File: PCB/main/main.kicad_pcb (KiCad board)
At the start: 2 copper layers, 100 x 100 mm, 46 parts, among them J1 Conn_01x33_Female, J2 Conn_01x33_Female, J3 Conn_01x33_Female, J4 Conn_01x33_Female, J5 USB_B_Micro, Q1 2N2222A, SW1 C13828, SW2 C13828, U1 TP4054, U2 MT3608L

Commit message: updated PCB & Assembly file
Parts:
- removed FTDI(UART)1: CH340C, CH340C:SOIC127P600X180-16N
- removed TSensor: LM75B, LM75BD:SOIC127P600X175-8N
- added FTDI1: CH340C, Package_SO:SOP-16_3.9x9.9mm_P1.27mm, F.Cu at (129.0, 78.8)
- added TempSensor1: LM75B, Package_SO:MSOP-8_3x3mm_P0.65mm, F.Cu at (133.5, 67.9)
- LDR1, LDR2, R1, R10, R11, R12, R13, R14, R15, R16, R17, R18, R19, R20, R5, R6, R7, R8, R9: footprint Resistor_SMD:R_0201_0603Metric -> Resistor_SMD:R_0603_1608Metric
- R2, R3, R4: value 100ohms -> 100; footprint Resistor_SMD:R_0201_0603Metric -> Resistor_SMD:R_0603_1608Metric
- moved J5 1.62 mm to (115.2, 92.7), turned to -90 degrees
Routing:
- net GND: track 83.8 -> 121.5 mm, vias 17 -> 18
- net +5V: track 0.00 -> 8.09 mm, vias 0 -> 2
- net /microcontroller_interfacing/USB Test Point: track 29.8 -> 23.0 mm, vias 0 -> 2
- net /PA8: track 135.9 -> 132.3 mm
- net USB D+: track 38.7 -> 35.1 mm
- net Net-(FTDI1-Pad13): track 67.5 -> 70.2 mm
- net /Power/Output: track 75.3 -> 77.8 mm
- net /PA9: track 50.4 -> 51.2 mm
- net /PA10: track 43.7 -> 44.5 mm
- net Net-(C4-Pad1): track 18.8 -> 19.6 mm
- net USB D-: track 34.6 -> 33.9 mm

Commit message: Updated PCB
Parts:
- LDR1, LDR2: footprint Resistor_SMD:R_0603_1608Metric -> Resistor_THT:R_Axial_DIN0204_L3.6mm_D1.6mm_P1.90mm_Vertical
- moved R19 4.74 mm to (129.5, 91.4)
- moved R14 2.89 mm to (149.9, 91.4)
- moved J5 2.68 mm to (112.6, 93.6)
- moved R20 2.19 mm to (134.6, 91.4)
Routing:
- net GND: track 121.5 -> 79.5 mm, vias 18 -> 0
- net Net-(D3-Pad2): track 35.3 -> 72.5 mm, vias 2 -> 4
- net Net-(BT1-Pad1): track 108.9 -> 134.2 mm, vias 4 -> 5
- net +5V: track 8.09 -> 24.5 mm, vias 2 -> 6
- net Net-(R6-Pad2): track 66.6 -> 80.2 mm
- net USB D+: track 35.1 -> 22.1 mm
- net /PA9: track 51.2 -> 38.8 mm
- net /Sensing/I2CBUS: track 72.7 -> 82.2 mm
- net Net-(L1-Pad1): track 8.44 -> 17.4 mm
- net /Power/Output: track 77.8 -> 84.4 mm
- net /PA8: track 132.3 -> 138.2 mm
- net /microcontroller_interfacing/EEPROM MODE TP: track 56.7 -> 51.2 mm, vias 2 -> 1
- net USB D-: track 33.9 -> 28.6 mm
- net Net-(R1-Pad1): track 13.4 -> 8.59 mm
- net Net-(LED1-Pad2): track 3.75 -> 8.10 mm
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- added copper zone on B.Cu, net +5V
- added copper zone on F.Cu, net GND
- removed copper zone on F.Cu, net +5V
- removed copper zone on B.Cu, net GND
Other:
- board text removed: "MT3608L"

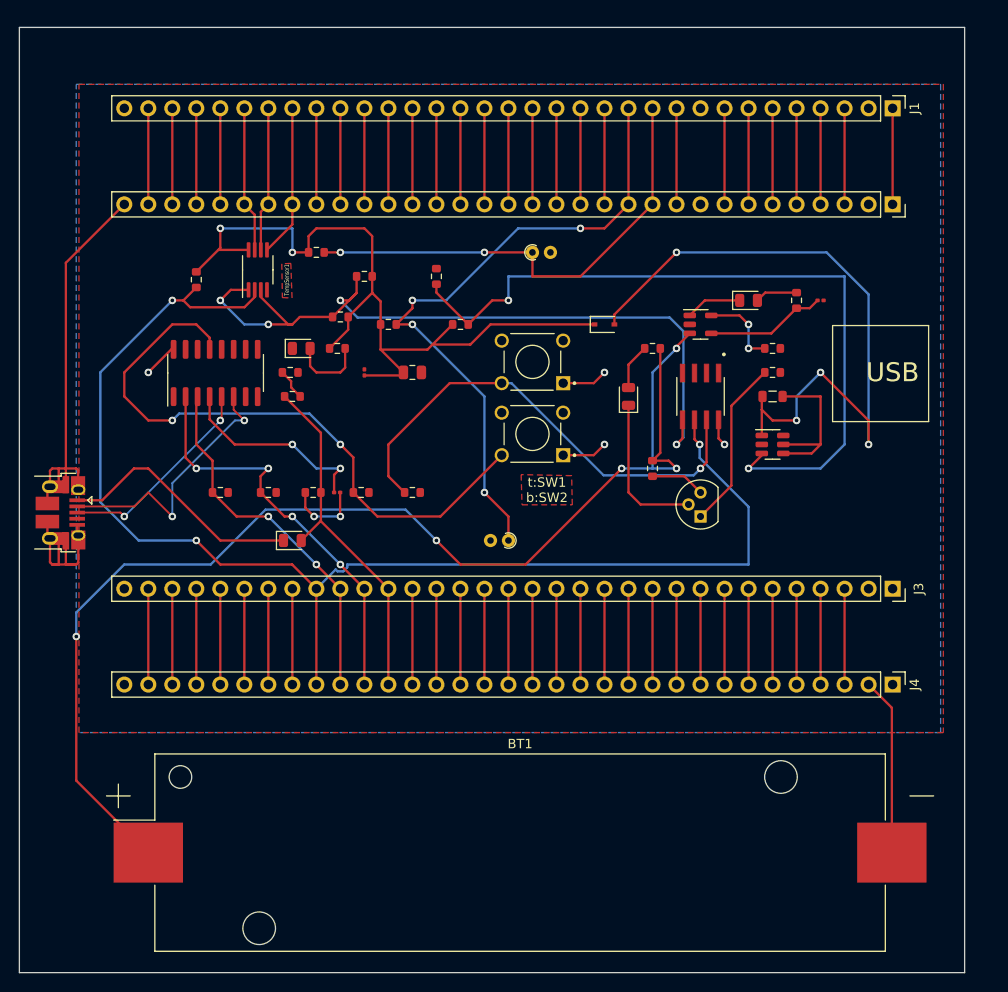
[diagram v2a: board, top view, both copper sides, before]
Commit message: rewired PCB and changed relevant footprints. production files regenerated
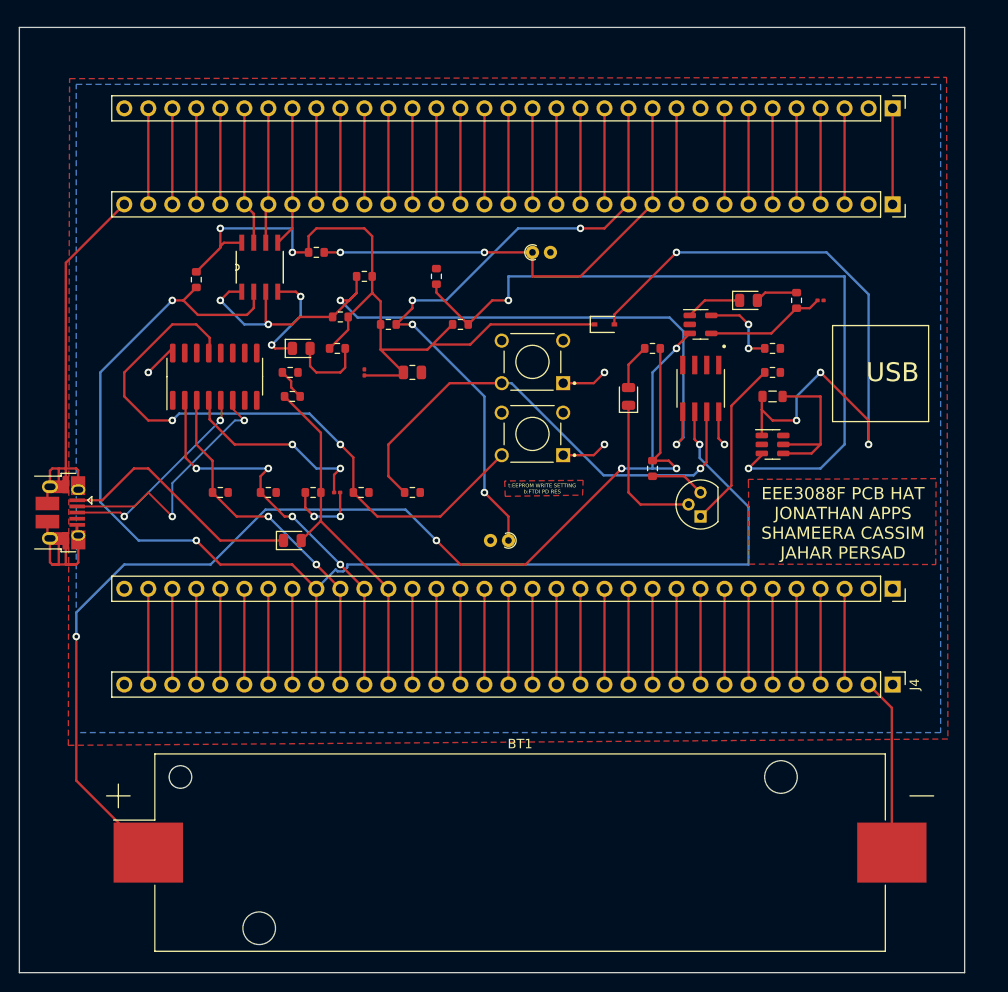
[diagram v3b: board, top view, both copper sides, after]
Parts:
- removed EEPROM1: AT24C256C-SSHL-T, SOIC127P600X175-8N:EEPROM
- removed FTDI1: CH340C, Package_SO:SOP-16_3.9x9.9mm_P1.27mm
- removed TempSensor1: LM75B, Package_SO:MSOP-8_3x3mm_P0.65mm
- added U3: LM75B, LM75BD:SOIC127P600X175-8N, F.Cu at (133.7, 67.6)
- added U4: AT24C256C-SSHL-T, SOIC127P600X175-8N:EEPROM, F.Cu at (180.4, 80.4)
- added U5: CH340C, Package_SO:SOP-16_3.9x9.9mm_P1.27mm, F.Cu at (128.9, 79.2)
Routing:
- net GND: track 79.5 -> 90.9 mm, vias 0 -> 2
- net /Sensing/I2CBUS: track 82.2 -> 79.6 mm
- net /PC5: track 16.1 -> 14.9 mm
- net /PA8: track 138.2 -> 139.3 mm
- net /PB0: track 15.3 -> 14.3 mm
- net /PB1: track 15.4 -> 14.6 mm
- net /Power/Output: track 84.4 -> 83.6 mm
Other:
- board text added: "EEE3088F PCB HAT JONATHAN APPS SHAMEERA CASSIM JAHAR PERSAD"
- board text added: "t:EEPROM WRITE SETTING b:FTDI PD RES"
- board text removed: "t:SW1 b:SW2"
